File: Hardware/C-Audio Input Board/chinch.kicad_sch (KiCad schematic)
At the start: 5 parts, among them J23 Chinch-In1, J24 +, J25 -, J26 GND, J27 Chinch1

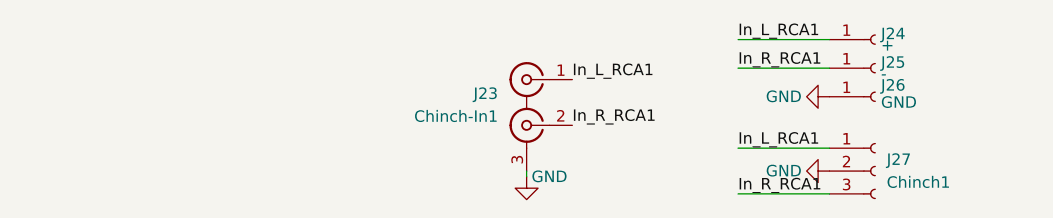
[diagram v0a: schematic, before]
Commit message: added mouser and reichelt numbers to BOM
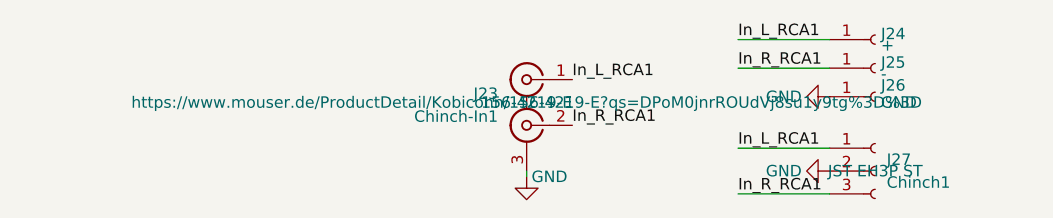
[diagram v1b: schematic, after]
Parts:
- J23: Mouser Link (none) -> https://www.mouser.de/ProductDetail/Kobiconn/156-4219-E?qs=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; Mouser Nr. (none) -> 156-4219-E; Mouser-Link (none) -> https://www.mouser.de/ProductDetail/Kobiconn/156-4219-E?qs=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
- J27: Reichelt Nr. (none) -> JST EH3P ST
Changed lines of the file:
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@@
 			)
 		)
-		(property "Datasheet" " ~"
+		(property "Datasheet" "https://www.mouser.de/datasheet/2/209/KC_2032021_1-2580140.pdf"
 			(at 78.74 62.23 0)
 			(effects
@@
 			)
 		)
-		(property "Mouser-Link" ""
+		(property "Mouser-Link" "https://www.mouser.de/ProductDetail/Kobiconn/156-4219-E?qs=DPoM0jnrROUdVj8su1y9tg%3D%3D"
 			(at 78.74 59.69 0)
 			(effects
@@
 				)
 				(hide yes)
+			)
+		)
+		(property "Mouser Link" "https://www.mouser.de/ProductDetail/Kobiconn/156-4219-E?qs=DPoM0jnrROUdVj8su1y9tg%3D%3D"
+			(at 78.74 59.69 0)
+			(effects
+				(font
+					(size 1.27 1.27)
+				)
+			)
+		)
+		(property "Mouser Nr." " 156-4219-E "
+			(at 78.74 59.69 0)
+			(effects
+				(font
+					(size 1.27 1.27)
+				)
 			)
 		)
@@
 			)
 		)
+		(property "Reichelt Nr." " JST EH3P ST"
+			(at 117.475 67.31 0)
+			(effects
+				(font
+					(size 1.27 1.27)
+				)
+			)
+		)
